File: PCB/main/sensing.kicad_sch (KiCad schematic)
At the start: 16 parts, among them IC1 LM358DT

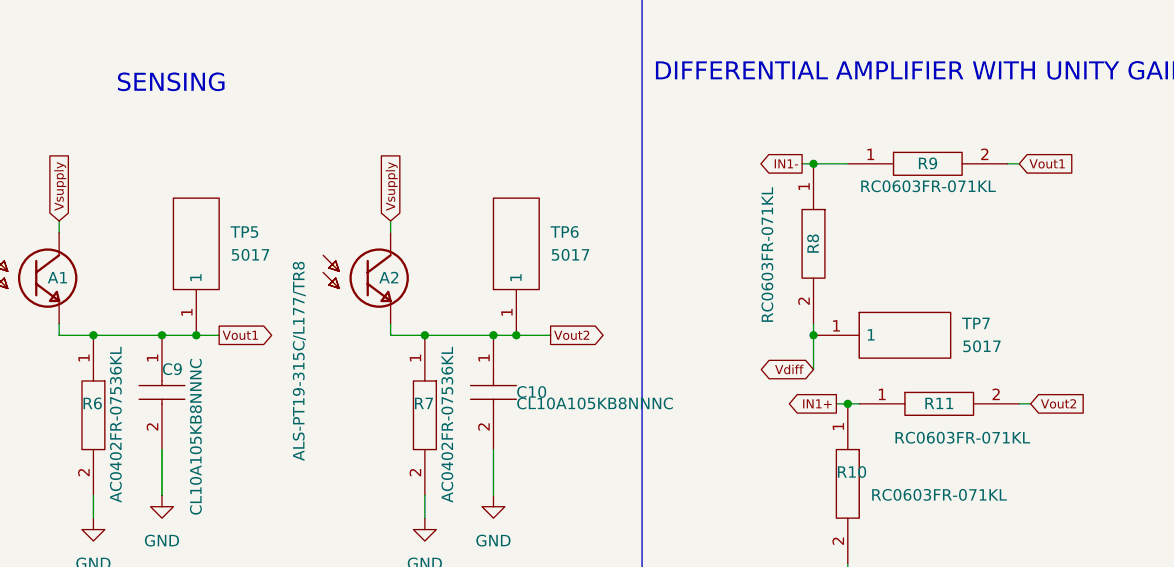
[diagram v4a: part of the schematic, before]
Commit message: changed power schematic
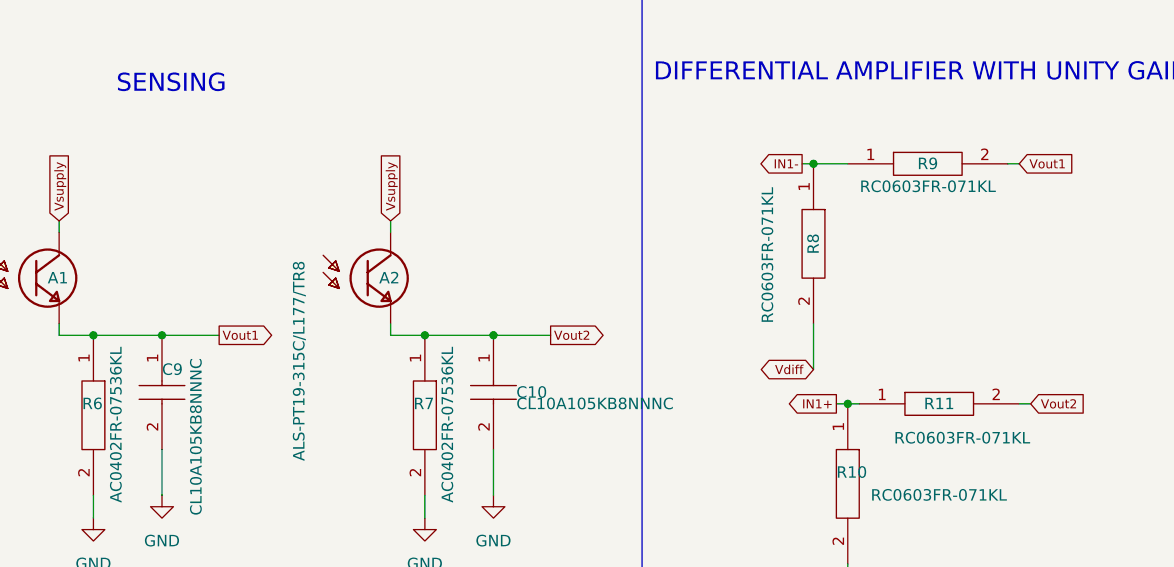
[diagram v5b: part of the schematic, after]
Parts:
- removed TP5, TP6, TP7: 5017, SamacSys_Parts_Power:5017, symbol SamacSys_Parts_power:5017
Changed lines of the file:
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@@
   (junction (at 82.55 133.35) (diameter 0) (color 0 0 0 0)
   )
-  (junction (at 86.36 133.35) (diameter 0) (color 0 0 0 0)
-  )
-  (junction (at 121.92 133.35) (diameter 0) (color 0 0 0 0)
-  )
   (junction (at 74.93 133.35) (diameter 0) (color 0 0 0 0)
   )
@@
   (junction (at 111.76 133.35) (diameter 0) (color 0 0 0 0)
   )
-  (junction (at 154.94 133.35) (diameter 0) (color 0 0 0 0)
-  )
-  (wire (pts (xy 86.36 133.35) (xy 88.9 133.35))
-    (stroke (width 0) (type default) (color 0 0 0 0))
-  )
   (wire (pts (xy 107.95 132.08) (xy 107.95 133.35))
     (stroke (width 0) (type default) (color 0 0 0 0))
@@
     (stroke (width 0) (type default) (color 0 0 0 0))
   )
-  (wire (pts (xy 121.92 133.35) (xy 125.73 133.35))
-    (stroke (width 0) (type default) (color 0 0 0 0))
-  )
-  (wire (pts (xy 154.94 133.35) (xy 154.94 137.16))
+  (wire (pts (xy 119.38 133.35) (xy 125.73 133.35))
+    (stroke (width 0) (type default) (color 0 0 0 0))
+  )
+  (wire (pts (xy 154.94 132.08) (xy 154.94 137.16))
     (stroke (width 0) (type default) (color 0 0 0 0))
   )
@@
     (stroke (width 0) (type default) (color 0 0 0 0))
   )
-  (wire (pts (xy 154.94 132.08) (xy 154.94 133.35))
-    (stroke (width 0) (type default) (color 0 0 0 0))
-  )
   (wire (pts (xy 25.4 115.57) (xy 25.4 116.84))
     (stroke (width 0) (type default) (color 0 0 0 0))
@@
     (stroke (width 0) (type default) (color 0 0 0 0))
   )
-  (wire (pts (xy 119.38 133.35) (xy 121.92 133.35))
-    (stroke (width 0) (type default) (color 0 0 0 0))
-  )
-  (wire (pts (xy 82.55 133.35) (xy 86.36 133.35))
+  (wire (pts (xy 82.55 133.35) (xy 88.9 133.35))
     (stroke (width 0) (type default) (color 0 0 0 0))
   )
@@
     (pin "2")
   )
-  (symbol (lib_id "SamacSys_Parts_power:5017") (at 86.36 133.35 90) (unit 1)
-    (in_bom yes) (on_board yes) (fields_autoplaced)
-    (property "Reference" "TP5" (id 0) (at 90.17 121.9199 90)
-      (effects (font (size 1.27 1.27)) (justify right))
-    )
-    (property "Value" "5017" (id 1) (at 90.17 124.4599 90)
-      (effects (font (size 1.27 1.27)) (justify right))
-    )
-    (property "Footprint" "SamacSys_Parts_Power:5017" (id 2) (at 83.82 116.84 0)
-      (effects (font (size 1.27 1.27)) (justify left) hide)
-    )
-    (property "Datasheet" "http://www.keyelco.com/product.cfm/product_id/1355" (id 3) (at 86.36 116.84 0)
-      (effects (font (size 1.27 1.27)) (justify left) hide)
-    )
-    (property "Description" "KEYSTONE - 5017 - TEST POINT, PCB, MINIATURE, SMT" (id 4) (at 88.9 116.84 0)
-      (effects (font (size 1.27 1.27)) (justify left) hide)
-    )
-    (property "Height" "" (id 5) (at 91.44 116.84 0)
-      (effects (font (size 1.27 1.27)) (justify left) hide)
-    )
-    (property "Manufacturer_Name" "Keystone Electronics" (id 6) (at 93.98 116.84 0)
-      (effects (font (size 1.27 1.27)) (justify left) hide)
-    )
-    (property "Manufacturer_Part_Number" "5017" (id 7) (at 96.52 116.84 0)
-      (effects (font (size 1.27 1.27)) (justify left) hide)
-    )
-    (property "Mouser Part Number" "534-5017" (id 8) (at 99.06 116.84 0)
-      (effects (font (size 1.27 1.27)) (justify left) hide)
-    )
-    (property "Mouser Price/Stock" "https://www.mouser.co.uk/ProductDetail/Keystone-Electronics/5017?qs=Rc9fedAPY0Oq34lsnTvuLg%3D%3D" (id 9) (at 101.6 116.84 0)
-      (effects (font (size 1.27 1.27)) (justify left) hide)
-    )
-    (property "Arrow Part Number" "" (id 10) (at 104.14 116.84 0)
-      (effects (font (size 1.27 1.27)) (justify left) hide)
-    )
-    (property "Arrow Price/Stock" "" (id 11) (at 106.68 116.84 0)
-      (effects (font (size 1.27 1.27)) (justify left) hide)
-    )
-    (property "Comment" "test point" (id 12) (at 86.36 133.35 0)
-      (effects (font (size 1.27 1.27)) hide)
-    )
-    (property "JLCPCB Part Number" "C238130" (id 13) (at 86.36 133.35 0)
-      (effects (font (size 1.27 1.27)) hide)
-    )
-    (property "LCSC" "C238130" (id 14) (at 86.36 133.35 0)
-      (effects (font (size 1.27 1.27)) hide)
-    )
-    (property "Price($)" "0.4796" (id 15) (at 86.36 133.35 0)
-      (effects (font (size 1.27 1.27)) hide)
-    )
-    (pin "1")
-  )
-  (symbol (lib_id "SamacSys_Parts_power:5017") (at 121.92 133.35 90) (unit 1)
-    (in_bom yes) (on_board yes) (fields_autoplaced)
-    (property "Reference" "TP6" (id 0) (at 125.73 121.9199 90)
-      (effects (font (size 1.27 1.27)) (justify right))
-    )
-    (property "Value" "5017" (id 1) (at 125.73 124.4599 90)
-      (effects (font (size 1.27 1.27)) (justify right))
-    )
-    (property "Footprint" "SamacSys_Parts_Power:5017" (id 2) (at 119.38 116.84 0)
-      (effects (font (size 1.27 1.27)) (justify left) hide)
-    )
-    (property "Datasheet" "http://www.keyelco.com/product.cfm/product_id/1355" (id 3) (at 121.92 116.84 0)
-      (effects (font (size 1.27 1.27)) (justify left) hide)
-    )
-    (property "Description" "KEYSTONE - 5017 - TEST POINT, PCB, MINIATURE, SMT" (id 4) (at 124.46 116.84 0)
-      (effects (font (size 1.27 1.27)) (justify left) hide)
-    )
-    (property "Height" "" (id 5) (at 127 116.84 0)
-      (effects (font (size 1.27 1.27)) (justify left) hide)
-    )
-    (property "Manufacturer_Name" "Keystone Electronics" (id 6) (at 129.54 116.84 0)
-      (effects (font (size 1.27 1.27)) (justify left) hide)
-    )
-    (property "Manufacturer_Part_Number" "5017" (id 7) (at 132.08 116.84 0)
-      (effects (font (size 1.27 1.27)) (justify left) hide)
-    )
-    (property "Mouser Part Number" "534-5017" (id 8) (at 134.62 116.84 0)
-      (effects (font (size 1.27 1.27)) (justify left) hide)
-    )
-    (property "Mouser Price/Stock" "https://www.mouser.co.uk/ProductDetail/Keystone-Electronics/5017?qs=Rc9fedAPY0Oq34lsnTvuLg%3D%3D" (id 9) (at 137.16 116.84 0)
-      (effects (font (size 1.27 1.27)) (justify left) hide)
-    )
-    (property "Arrow Part Number" "" (id 10) (at 139.7 116.84 0)
-      (effects (font (size 1.27 1.27)) (justify left) hide)
-    )
-    (property "Arrow Price/Stock" "" (id 11) (at 142.24 116.84 0)
-      (effects (font (size 1.27 1.27)) (justify left) hide)
-    )
-    (property "Comment" "test point" (id 12) (at 121.92 133.35 0)
-      (effects (font (size 1.27 1.27)) hide)
-    )
-    (property "JLCPCB Part Number" "C238130" (id 13) (at 121.92 133.35 0)
-      (effects (font (size 1.27 1.27)) hide)
-    )
-    (property "LCSC" "C238130" (id 14) (at 121.92 133.35 0)
-      (effects (font (size 1.27 1.27)) hide)
-    )
-    (property "Price($)" "0.4796" (id 15) (at 121.92 133.35 0)
-      (effects (font (size 1.27 1.27)) hide)
-    )
-    (pin "1")
-  )
   (symbol (lib_id "power:GND") (at 82.55 151.13 0) (unit 1)
     (in_bom yes) (on_board yes) (fields_autoplaced)
@@
       (effects (font (size 1.27 1.27)) hide)
     )
-    (pin "1")
-  )
-  (symbol (lib_id "SamacSys_Parts_power:5017") (at 154.94 133.35 0) (unit 1)
-    (in_bom yes) (on_board yes) (fields_autoplaced)
-    (property "Reference" "TP7" (id 0) (at 171.45 132.0799 0)
-      (effects (font (size 1.27 1.27)) (justify left))
-    )
-    (property "Value" "5017" (id 1) (at 171.45 134.6199 0)
-      (effects (font (size 1.27 1.27)) (justify left))
-    )
-    (property "Footprint" "SamacSys_Parts_Power:5017" (id 2) (at 171.45 130.81 0)
-      (effects (font (size 1.27 1.27)) (justify left) hide)
-    )
-    (property "Datasheet" "http://www.keyelco.com/product.cfm/product_id/1355" (id 3) (at 171.45 133.35 0)
-      (effects (font (size 1.27 1.27)) (justify left) hide)
-    )
-    (property "Description" "KEYSTONE - 5017 - TEST POINT, PCB, MINIATURE, SMT" (id 4) (at 171.45 135.89 0)
-      (effects (font (size 1.27 1.27)) (justify left) hide)
-    )
-    (property "Height" "" (id 5) (at 171.45 138.43 0)
-      (effects (font (size 1.27 1.27)) (justify left) hide)
-    )
-    (property "Manufacturer_Name" "Keystone Electronics" (id 6) (at 171.45 140.97 0)
-      (effects (font (size 1.27 1.27)) (justify left) hide)
-    )
-    (property "Manufacturer_Part_Number" "5017" (id 7) (at 171.45 143.51 0)
-      (effects (font (size 1.27 1.27)) (justify left) hide)
-    )
-    (property "Mouser Part Number" "534-5017" (id 8) (at 171.45 146.05 0)
-      (effects (font (size 1.27 1.27)) (justify left) hide)
-    )
-    (property "Mouser Price/Stock" "https://www.mouser.co.uk/ProductDetail/Keystone-Electronics/5017?qs=Rc9fedAPY0Oq34lsnTvuLg%3D%3D" (id 9) (at 171.45 148.59 0)
-      (effects (font (size 1.27 1.27)) (justify left) hide)
-    )
-    (property "Arrow Part Number" "" (id 10) (at 171.45 151.13 0)
-      (effects (font (size 1.27 1.27)) (justify left) hide)
-    )
-    (property "Arrow Price/Stock" "" (id 11) (at 171.45 153.67 0)
-      (effects (font (size 1.27 1.27)) (justify left) hide)
-    )
-    (property "Comment" "test point" (id 12) (at 154.94 133.35 0)
-      (effects (font (size 1.27 1.27)) hide)
-    )
-    (property "JLCPCB Part Number" "C238130" (id 13) (at 154.94 133.35 0)
-      (effects (font (size 1.27 1.27)) hide)
-    )
-    (property "LCSC" "C238130" (id 14) (at 154.94 133.35 0)
-      (effects (font (size 1.27 1.27)) hide)
-    )
-    (property "Price($)" "0.4796" (id 15) (at 154.94 133.35 0)
-      (effects (font (size 1.27 1.27)) hide)
-    )

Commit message: generated new files
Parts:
- added J15: MTP125-1103S1, SamacSys_Parts:HDRV3W64P0X254_1X3_762X250X885P, symbol SamacSys_Parts_power:MTP125-1103S1
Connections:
- net Vout1: now also J15.1; no longer A1.2, C9.1, R6.1, R9.2
- net Vout2: now also J15.2
- new net Vout: A1.2, C9.1, J15.3, R6.1, R9.2
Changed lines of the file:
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@@
+    (stroke (width 0) (type default) (color 0 0 0 0))
+  )
+  (wire (pts (xy 93.98 177.165) (xy 79.375 177.165))
     (stroke (width 0) (type default) (color 0 0 0 0))
   )
@@
     (stroke (width 0) (type default) (color 0 0 0 0))
   )
+  (wire (pts (xy 96.52 171.45) (xy 96.52 179.705))
+    (stroke (width 0) (type default) (color 0 0 0 0))
+  )
+  (wire (pts (xy 99.06 179.705) (xy 112.395 179.705))
+    (stroke (width 0) (type default) (color 0 0 0 0))
+  )
+  (wire (pts (xy 79.375 177.165) (xy 79.375 175.26))
+    (stroke (width 0) (type default) (color 0 0 0 0))
+  )
   (wire (pts (xy 25.4 115.57) (xy 25.4 116.84))
     (stroke (width 0) (type default) (color 0 0 0 0))
@@
   )
   (wire (pts (xy 158.75 160.02) (xy 158.75 158.75))
+    (stroke (width 0) (type default) (color 0 0 0 0))
+  )
+  (wire (pts (xy 93.98 179.705) (xy 93.98 177.165))
     (stroke (width 0) (type default) (color 0 0 0 0))
   )
@@
     )
   )
+  (global_label "Vout" (shape input) (at 79.375 175.26 90) (fields_autoplaced)
+    (effects (font (size 1.27 1.27)) (justify left))
+    (property "Intersheet References" "${INTERSHEET_REFS}" (id 0) (at 79.2956 168.7345 90)
+      (effects (font (size 1.27 1.27)) (justify left) hide)
+    )
+  )
   (global_label "Vsupply" (shape output) (at 276.86 114.3 90) (fields_autoplaced)
     (effects (font (size 1 1)) (justify left))
@@
     )
   )
-  (global_label "Vout1" (shape input) (at 177.8 114.3 0) (fields_autoplaced)
+  (global_label "Vout" (shape input) (at 177.8 114.3 0) (fields_autoplaced)
     (effects (font (size 1 1)) (justify left))
-    (property "Intersheet References" "${INTERSHEET_REFS}" (id 0) (at 183.8905 114.2375 0)
+    (property "Intersheet References" "${INTERSHEET_REFS}" (id 0) (at 182.9381 114.2375 0)
       (effects (font (size 1 1)) (justify left) hide)
     )
@@
     )
   )
+  (global_label "Vout1" (shape input) (at 112.395 179.705 0) (fields_autoplaced)
+    (effects (font (size 1.27 1.27)) (justify left))
+    (property "Intersheet References" "${INTERSHEET_REFS}" (id 0) (at 120.13 179.6256 0)
+      (effects (font (size 1.27 1.27)) (justify left) hide)
+    )
+  )
   (global_label "Vsupply" (shape input) (at 107.95 120.65 90) (fields_autoplaced)
     (effects (font (size 1 1)) (justify left))
@@
     )
   )
-  (global_label "Vout1" (shape output) (at 88.9 133.35 0) (fields_autoplaced)
+  (global_label "Vout2" (shape input) (at 96.52 171.45 90) (fields_autoplaced)
+    (effects (font (size 1.27 1.27)) (justify left))
+    (property "Intersheet References" "${INTERSHEET_REFS}" (id 0) (at 96.4406 163.715 90)
+      (effects (font (size 1.27 1.27)) (justify left) hide)
+    )
+  )
+  (global_label "Vout" (shape output) (at 88.9 133.35 0) (fields_autoplaced)
     (effects (font (size 1 1)) (justify left))
-    (property "Intersheet References" "${INTERSHEET_REFS}" (id 0) (at 94.9905 133.2875 0)
+    (property "Intersheet References" "${INTERSHEET_REFS}" (id 0) (at 94.0381 133.2875 0)
       (effects (font (size 1 1)) (justify left) hide)
     )
@@
     (pin "1")
   )
+  (symbol (lib_id "SamacSys_Parts_power:MTP125-1103S1") (at 99.06 179.705 270) (unit 1)
+    (in_bom yes) (on_board yes) (fields_autoplaced)
+    (property "Reference" "J15" (id 0) (at 103.505 188.5949 90)
+      (effects (font (size 1.27 1.27)) (justify left))
+    )
+    (property "Value" "MTP125-1103S1" (id 1) (at 103.505 191.1349 90)
+      (effects (font (size 1.27 1.27)) (justify left))
+    )
+    (property "Footprint" "SamacSys_Parts:HDRV3W64P0X254_1X3_762X250X885P" (id 2) (at 101.6 196.215 0)
+      (effects (font (size 1.27 1.27)) (justify left) hide)
+    )
+    (property "Datasheet" "https://datasheet.lcsc.com/szlcsc/1901241805_MINTRON-MTP125-1103S1_C358685.pdf" (id 3) (at 99.06 196.215 0)
+      (effects (font (size 1.27 1.27)) (justify left) hide)
+    )
+    (property "Description" "Through Hole,P=2.54mm Pin Header & Female Header" (id 4) (at 96.52 196.215 0)
+      (effects (font (size 1.27 1.27)) (justify left) hide)
+    )
+    (property "Height" "8.85" (id 5) (at 93.98 196.215 0)
+      (effects (font (size 1.27 1.27)) (justify left) hide)
+    )
+    (property "Manufacturer_Name" "MINTRON" (id 6) (at 91.44 196.215 0)
+      (effects (font (size 1.27 1.27)) (justify left) hide)
+    )
+    (property "Manufacturer_Part_Number" "MTP125-1103S1" (id 7) (at 88.9 196.215 0)
+      (effects (font (size 1.27 1.27)) (justify left) hide)
+    )
+    (property "Mouser Part Number" "" (id 8) (at 86.36 196.215 0)
+      (effects (font (size 1.27 1.27)) (justify left) hide)
+    )
+    (property "Mouser Price/Stock" "" (id 9) (at 83.82 196.215 0)
+      (effects (font (size 1.27 1.27)) (justify left) hide)
+    )
+    (property "Arrow Part Number" "" (id 10) (at 81.28 196.215 0)
+      (effects (font (size 1.27 1.27)) (justify left) hide)
+    )
+    (property "Arrow Price/Stock" "" (id 11) (at 78.74 196.215 0)
+      (effects (font (size 1.27 1.27)) (justify left) hide)
+    )
+    (property "Comment" "pin header (3x1)" (id 12) (at 99.06 179.705 0)
+      (effects (font (size 1.27 1.27)) hide)
+    )
+    (property "LCSC" "C358685" (id 13) (at 99.06 179.705 0)
+      (effects (font (size 1.27 1.27)) hide)
+    )
+    (pin "1")
+    (pin "2")
+    (pin "3")
+  )
   (symbol (lib_id "power:GND") (at 111.76 153.67 0) (unit 1)
